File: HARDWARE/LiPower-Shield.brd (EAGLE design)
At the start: 59.7 x 53.3 mm, 51 parts, among them U1 MAX17043G+U, U2 TPS61200, U3 MCP73831, U4 ARDUINO_R3_SHIELD, X1 USBSMD

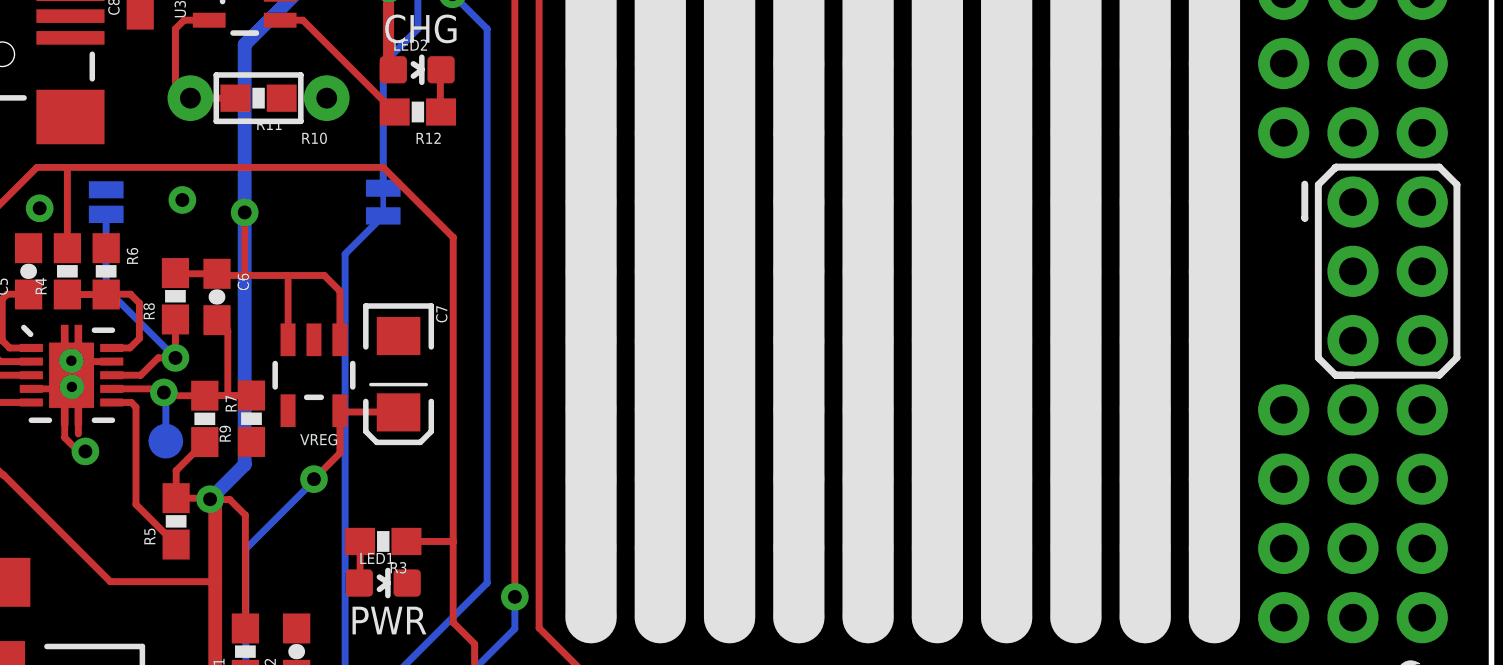
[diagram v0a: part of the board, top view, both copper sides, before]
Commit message: Changed res values on the UVLO line.
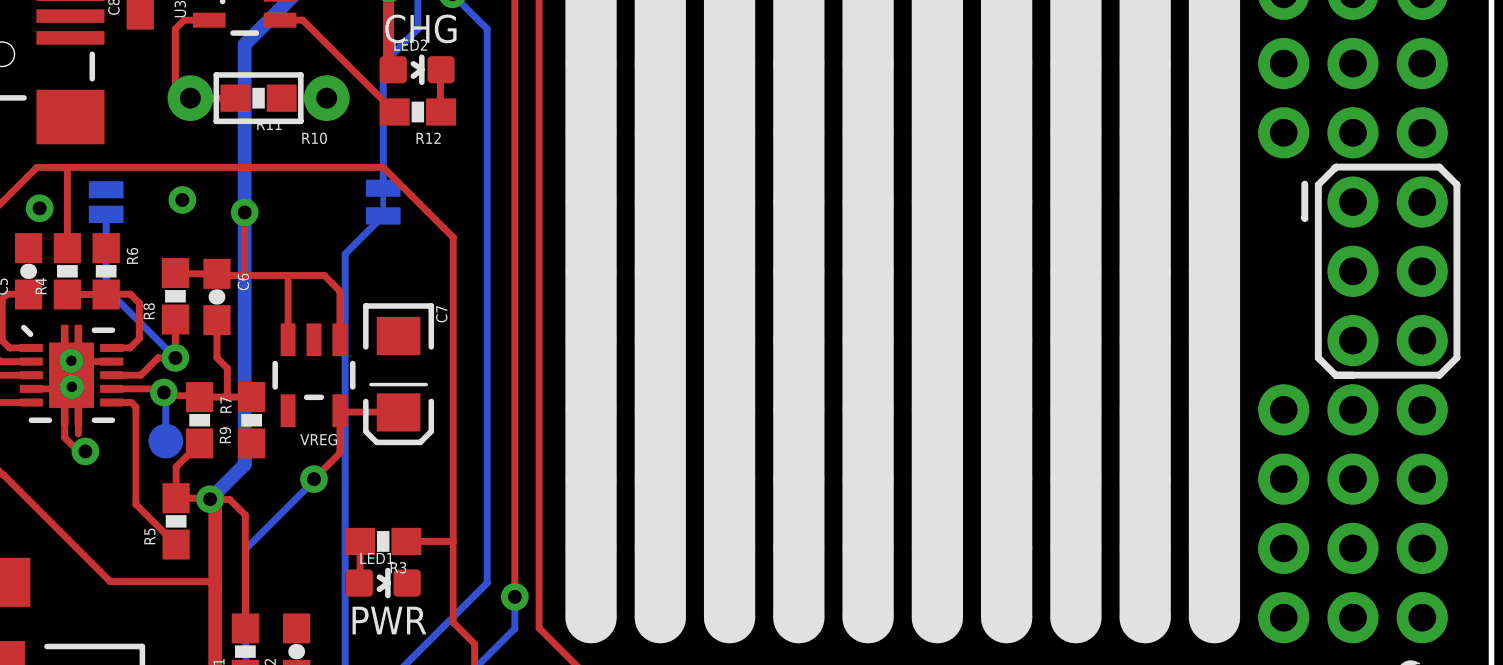
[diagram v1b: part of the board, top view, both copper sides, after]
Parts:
- R7: value 2M -> 2.2M
- R9: value 220k -> 200k
- moved R7 0.19 mm to (12.3, 22.5)
- moved R9 0.06 mm to (14.2, 22.5)
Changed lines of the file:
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@@
 <layer number="47" name="Measures" color="7" fill="1" visible="no" active="yes"/>
 <layer number="48" name="Document" color="7" fill="1" visible="no" active="yes"/>
-<layer number="49" name="Reference" color="7" fill="1" visible="yes" active="yes"/>
+<layer number="49" name="Reference" color="7" fill="1" visible="no" active="yes"/>
 <layer number="50" name="dxf" color="7" fill="1" visible="no" active="yes"/>
 <layer number="51" name="tDocu" color="6" fill="1" visible="yes" active="yes"/>
@@
 <wire x1="58.422540625" y1="31.115" x2="57.774840625" y2="31.7627" width="0.254" layer="21"/>
 <wire x1="57.774840625" y1="31.7627" x2="53.9877" y2="31.7627" width="0.254" layer="21"/>
-<wire x1="53.9877" y1="31.7627" x2="53.975" y2="31.75" width="0.254" layer="21"/>
-<wire x1="53.975" y1="31.75" x2="53.94198125" y2="31.71698125" width="0.254" layer="21"/>
+<wire x1="53.9877" y1="31.7627" x2="53.94198125" y2="31.71698125" width="0.254" layer="21"/>
 <wire x1="53.94198125" y1="31.71698125" x2="53.93944375" y2="31.71698125" width="0.254" layer="21"/>
 <wire x1="26.67" y1="40.64" x2="26.67" y2="15.24" width="1.8796" layer="21"/>
@@
 <attribute name="VALUE" value="0.1uF" x="6.0452" y="27.94" size="1.778" layer="27" rot="R90" display="off"/>
 </element>
-<element name="R7" library="SparkFun-Resistors" package="0603-RES" value="2M" x="12.506959375" y="22.5298" rot="R270">
-<attribute name="PROD_ID" value="RES-10054" x="12.506959375" y="22.5298" size="1.778" layer="27" rot="R270" display="off"/>
-<attribute name="VALUE" value="2.0M" x="12.506959375" y="22.5298" size="1.778" layer="27" rot="R270" display="off"/>
-</element>
-<element name="R9" library="SparkFun-Resistors" package="0603-RES" value="220k" x="14.218921875" y="22.534878125" rot="R90">
-<attribute name="PROD_ID" value="RES-08969" x="14.218921875" y="22.534878125" size="1.778" layer="27" rot="R90" display="off"/>
-<attribute name="VALUE" value="220k" x="14.218921875" y="22.534878125" size="1.778" layer="27" rot="R90" display="off"/>
-</element>
 <element name="R6" library="SparkFun-Resistors" package="0603-RES" value="220k" x="8.89" y="27.94" rot="R270">
 <attribute name="PROD_ID" value="RES-08969" x="8.89" y="27.94" size="1.778" layer="27" rot="R270" display="off"/>
@@
 <element name="JP8" library="SparkFun-Connectors" package="1X08_NO_SILK" value="" x="36.83" y="44.45"/>
 <element name="S2" library="SparkFun-Electromechanical" package="SWITCH-SPST-SMD-A" value="" x="9.652" y="1.778" rot="R180"/>
+<element name="R9" library="SparkFun-Resistors" package="0603-RES" value="200k" x="14.224" y="22.479" rot="R90">
+<attribute name="PROD_ID" value="RES-09385" x="14.224" y="22.479" size="1.778" layer="27" font="vector" ratio="15" rot="R90" display="off"/>
+</element>
+<element name="R7" library="SparkFun-Resistors" package="0603-RES" value="2.2M" x="12.319" y="22.479" rot="R270">
+<attribute name="PROD_ID" value="RES-09288" x="12.319" y="22.479" size="1.778" layer="27" font="vector" ratio="15" rot="R270" display="off"/>
+</element>
 </elements>
 <signals>
@@
 <contactref element="C5" pad="2"/>
 <contactref element="U2" pad="9"/>
-<contactref element="R9" pad="1"/>
 <contactref element="R6" pad="1"/>
 <contactref element="SJ2" pad="1"/>
@@
 <via x="7.61238125" y="24.66085625" extent="1-16" drill="0.381"/>
 <via x="7.6327" y="23.70328125" extent="1-16" drill="0.381"/>
+<contactref element="R9" pad="1"/>
 </signal>
 <signal name="PROG">
@@
 <contactref element="U2" pad="5"/>
 <contactref element="C6" pad="1"/>
-<contactref element="R7" pad="2"/>
 <contactref element="C4" pad="1"/>
 <contactref element="L1" pad="P$2"/>
@@
 <wire x1="13.97" y1="30.099" x2="13.97" y2="27.7876" width="0.254" layer="1"/>
 <wire x1="14.00048125" y1="30.06851875" x2="13.97" y2="30.099" width="0.508" layer="16"/>
-<wire x1="11.4554" y1="19.6206" x2="11.4554" y2="20.628240625" width="0.254" layer="1"/>
-<wire x1="11.4554" y1="20.628240625" x2="12.506959375" y2="21.6798" width="0.254" layer="1"/>
+<wire x1="11.4554" y1="19.6206" x2="11.4554" y2="20.7654" width="0.254" layer="1"/>
 <wire x1="12.7" y1="19.5834" x2="13.97" y2="20.8534" width="0.508" layer="16"/>
 <wire x1="13.97" y1="20.8534" x2="13.97" y2="30.099" width="0.508" layer="16"/>
@@
 <wire x1="12.7127" y1="19.5707" x2="12.7" y2="19.5834" width="0.254" layer="1"/>
 <wire x1="12.7" y1="19.5834" x2="12.7" y2="19.6206" width="0.254" layer="1"/>
+<contactref element="R7" pad="2"/>
+<wire x1="11.4554" y1="20.7654" x2="12.319" y2="21.629" width="0.254" layer="1"/>
 </signal>
 <signal name="N$2">
@@
 <contactref element="U2" pad="7"/>
 <contactref element="C6" pad="2"/>
-<contactref element="R7" pad="1"/>
-<contactref element="R9" pad="2"/>
-<wire x1="12.256759375" y1="23.63" x2="12.506959375" y2="23.3798" width="0.254" layer="1" curve="-90"/>
 <contactref element="TP1" pad="P$1"/>
 <via x="11.005821875" y="23.4975375" extent="1-16" drill="0.508"/>
-<wire x1="12.256759375" y1="23.63" x2="12.124296875" y2="23.4975375" width="0.254" layer="1"/>
 <wire x1="9.095" y1="23.63" x2="10.873359375" y2="23.63" width="0.254" layer="1"/>
 <wire x1="10.873359375" y1="23.63" x2="11.005821875" y2="23.4975375" width="0.254" layer="1"/>
 <wire x1="11.005821875" y1="23.4975375" x2="11.123559375" y2="23.3798" width="0.254" layer="1"/>
-<wire x1="11.123559375" y1="23.3798" x2="12.506959375" y2="23.3798" width="0.254" layer="1"/>
-<wire x1="12.506959375" y1="23.3798" x2="12.5120375" y2="23.384878125" width="0.254" layer="1"/>
-<wire x1="12.5120375" y1="23.384878125" x2="13.350240625" y2="23.384878125" width="0.254" layer="1"/>
-<wire x1="13.350240625" y1="23.384878125" x2="14.218921875" y2="23.384878125" width="0.254" layer="1"/>
-<wire x1="12.954" y1="26.1502" x2="13.350240625" y2="25.753959375" width="0.254" layer="1"/>
-<wire x1="13.350240625" y1="25.753959375" x2="13.350240625" y2="23.384878125" width="0.254" layer="1"/>
 <wire x1="11.076940625" y1="21.71191875" x2="11.076940625" y2="23.42641875" width="0.254" layer="16"/>
 <wire x1="11.076940625" y1="23.42641875" x2="11.005821875" y2="23.4975375" width="0.254" layer="16"/>
+<contactref element="R9" pad="2"/>
+<wire x1="14.1732" y1="23.3798" x2="14.224" y2="23.329" width="0.254" layer="1"/>
+<wire x1="12.954" y1="26.1502" x2="12.954" y2="24.765" width="0.254" layer="1"/>
+<wire x1="12.954" y1="24.765" x2="13.335" y2="24.384" width="0.254" layer="1"/>
+<contactref element="R7" pad="1"/>
+<wire x1="11.123559375" y1="23.3798" x2="12.2682" y2="23.3798" width="0.254" layer="1"/>
+<wire x1="12.2682" y1="23.3798" x2="12.319" y2="23.329" width="0.254" layer="1"/>
+<wire x1="12.319" y1="23.329" x2="13.335" y2="23.329" width="0.254" layer="1"/>
+<wire x1="13.335" y1="23.329" x2="14.224" y2="23.329" width="0.254" layer="1"/>
+<wire x1="13.335" y1="24.384" x2="13.335" y2="23.329" width="0.254" layer="1"/>
 </signal>
 <signal name="FB">

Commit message: Moved Sparkfun silk
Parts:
- moved LOGO2 2.55 mm to (2.54, 12.4)
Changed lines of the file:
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@@
 <element name="TP1" library="SparkFun-Passives" package="PAD.03X.05" value="TEST-POINT3X5" x="11.076940625" y="21.71191875" rot="MR0"/>
 <element name="LOGO1" library="SparkFun-Aesthetics" package="OSHW-LOGO-S" value="OSHW-LOGOS" x="2.092959375" y="30.5562"/>
-<element name="LOGO2" library="SparkFun-Aesthetics" package="SFE_LOGO_NAME_FLAME_.2" value="SFE_LOGO_NAME_FLAME.2_INCH" x="5.08" y="12.7" rot="MR90"/>
+<element name="LOGO2" library="SparkFun-Aesthetics" package="SFE_LOGO_NAME_FLAME_.2" value="SFE_LOGO_NAME_FLAME.2_INCH" x="2.54" y="12.446" rot="MR90"/>
 <element name="U$2" library="SparkFun-Electromechanical" package="STAND-OFF-TIGHT" value="" x="57.15" y="6.35"/>
 <element name="U$3" library="SparkFun-Electromechanical" package="STAND-OFF-TIGHT" value="" x="5.08" y="50.8"/>

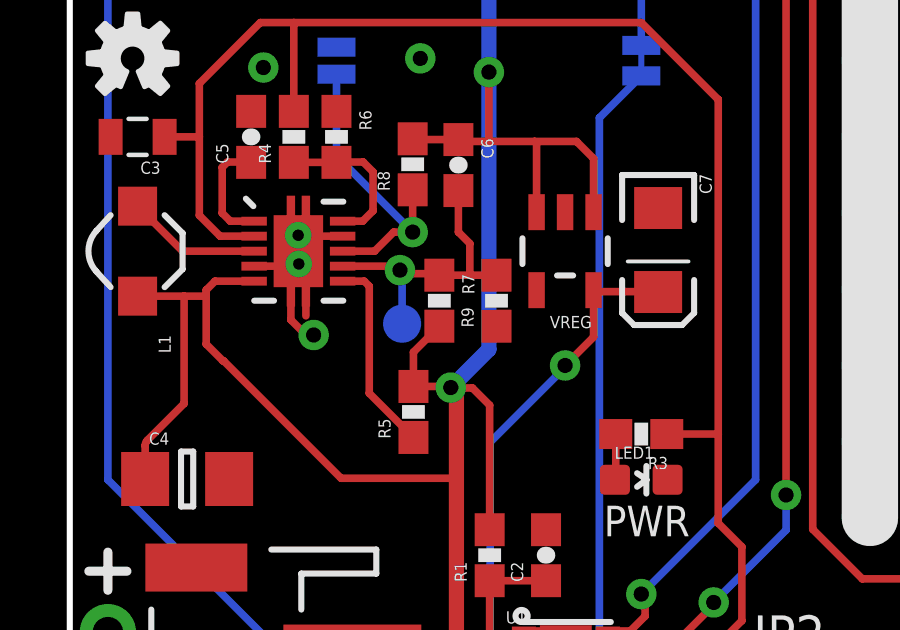
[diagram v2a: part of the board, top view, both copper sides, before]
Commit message: Changed r7 back to 2m
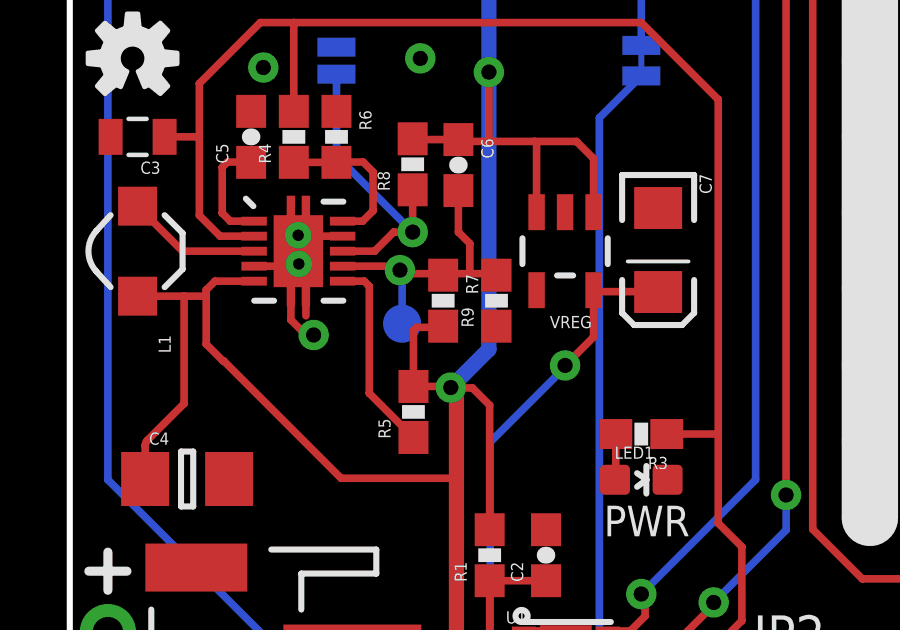
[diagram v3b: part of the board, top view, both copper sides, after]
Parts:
- R7: value 2.2M -> 2.0M
- moved R7 0.13 mm to (12.4, 22.5)
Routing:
- net VBATT: track 87.6 -> 88.1 mm
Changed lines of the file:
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@@
 <attribute name="PROD_ID" value="RES-09385" x="14.224" y="22.479" size="1.778" layer="27" font="vector" ratio="15" rot="R90" display="off"/>
 </element>
-<element name="R7" library="SparkFun-Resistors" package="0603-RES" value="2.2M" x="12.319" y="22.479" rot="R270">
-<attribute name="PROD_ID" value="RES-09288" x="12.319" y="22.479" size="1.778" layer="27" font="vector" ratio="15" rot="R270" display="off"/>
+<element name="R7" library="SparkFun-Resistors" package="0603-RES" value="2.0M" x="12.446" y="22.479" rot="R270">
+<attribute name="PROD_ID" value="RES-10054" x="12.446" y="22.479" size="1.778" layer="27" font="vector" ratio="15" rot="R270" display="off"/>
 </element>
 </elements>
@@
 <wire x1="13.97" y1="30.099" x2="13.97" y2="27.7876" width="0.254" layer="1"/>
 <wire x1="14.00048125" y1="30.06851875" x2="13.97" y2="30.099" width="0.508" layer="16"/>
-<wire x1="11.4554" y1="19.6206" x2="11.4554" y2="20.7654" width="0.254" layer="1"/>
 <wire x1="12.7" y1="19.5834" x2="13.97" y2="20.8534" width="0.508" layer="16"/>
 <wire x1="13.97" y1="20.8534" x2="13.97" y2="30.099" width="0.508" layer="16"/>
@@
 <wire x1="12.7" y1="19.5834" x2="12.7" y2="19.6206" width="0.254" layer="1"/>
 <contactref element="R7" pad="2"/>
-<wire x1="11.4554" y1="20.7654" x2="12.319" y2="21.629" width="0.254" layer="1"/>
+<wire x1="11.4554" y1="19.6206" x2="11.4554" y2="21.4884" width="0.254" layer="1"/>
+<wire x1="11.4554" y1="21.4884" x2="11.557" y2="21.59" width="0.254" layer="1"/>
+<wire x1="11.557" y1="21.59" x2="12.407" y2="21.59" width="0.254" layer="1"/>
+<wire x1="12.407" y1="21.59" x2="12.446" y2="21.629" width="0.254" layer="1"/>
 </signal>
 <signal name="N$2">
@@
 <wire x1="12.954" y1="24.765" x2="13.335" y2="24.384" width="0.254" layer="1"/>
 <contactref element="R7" pad="1"/>
-<wire x1="11.123559375" y1="23.3798" x2="12.2682" y2="23.3798" width="0.254" layer="1"/>
-<wire x1="12.2682" y1="23.3798" x2="12.319" y2="23.329" width="0.254" layer="1"/>
-<wire x1="12.319" y1="23.329" x2="13.335" y2="23.329" width="0.254" layer="1"/>
-<wire x1="13.335" y1="23.329" x2="14.224" y2="23.329" width="0.254" layer="1"/>
-<wire x1="13.335" y1="24.384" x2="13.335" y2="23.329" width="0.254" layer="1"/>
+<wire x1="11.123559375" y1="23.3798" x2="12.3952" y2="23.3798" width="0.254" layer="1"/>
+<wire x1="12.3952" y1="23.3798" x2="12.446" y2="23.329" width="0.254" layer="1"/>
+<wire x1="13.335" y1="23.3798" x2="12.4968" y2="23.3798" width="0.254" layer="1"/>
+<wire x1="12.4968" y1="23.3798" x2="12.446" y2="23.329" width="0.254" layer="1"/>
+<wire x1="14.1732" y1="23.3798" x2="13.335" y2="23.3798" width="0.254" layer="1"/>
+<wire x1="13.335" y1="23.3798" x2="13.335" y2="24.384" width="0.254" layer="1"/>
 </signal>
 <signal name="FB">
